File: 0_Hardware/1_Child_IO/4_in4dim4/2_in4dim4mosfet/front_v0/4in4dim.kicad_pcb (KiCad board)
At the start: 2 copper layers, 100.1 x 41.9 mm, 40 parts, among them IC1 ATTINY48-A, P1 CONN_8X2, P2 CONN_2, P3 CONN_2, P4 CONN_2, P5 CONN_2, P6 CONN_2, Q1 PNP, Q2 PNP, Q3 PNP, Q4 PNP, SW1 SKQGAKE010

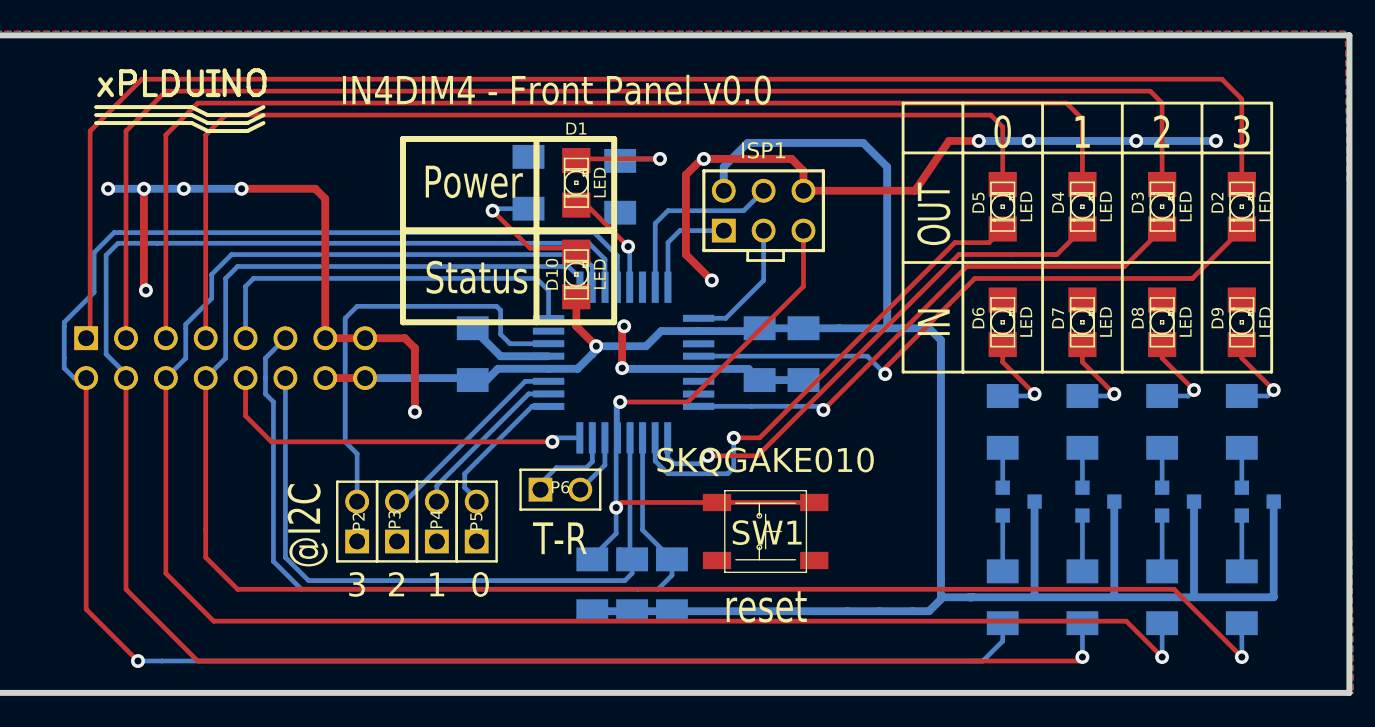
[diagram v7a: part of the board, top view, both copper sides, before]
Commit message: IN4DIM4: remplacement empreinte PNP par SOT-23 standard
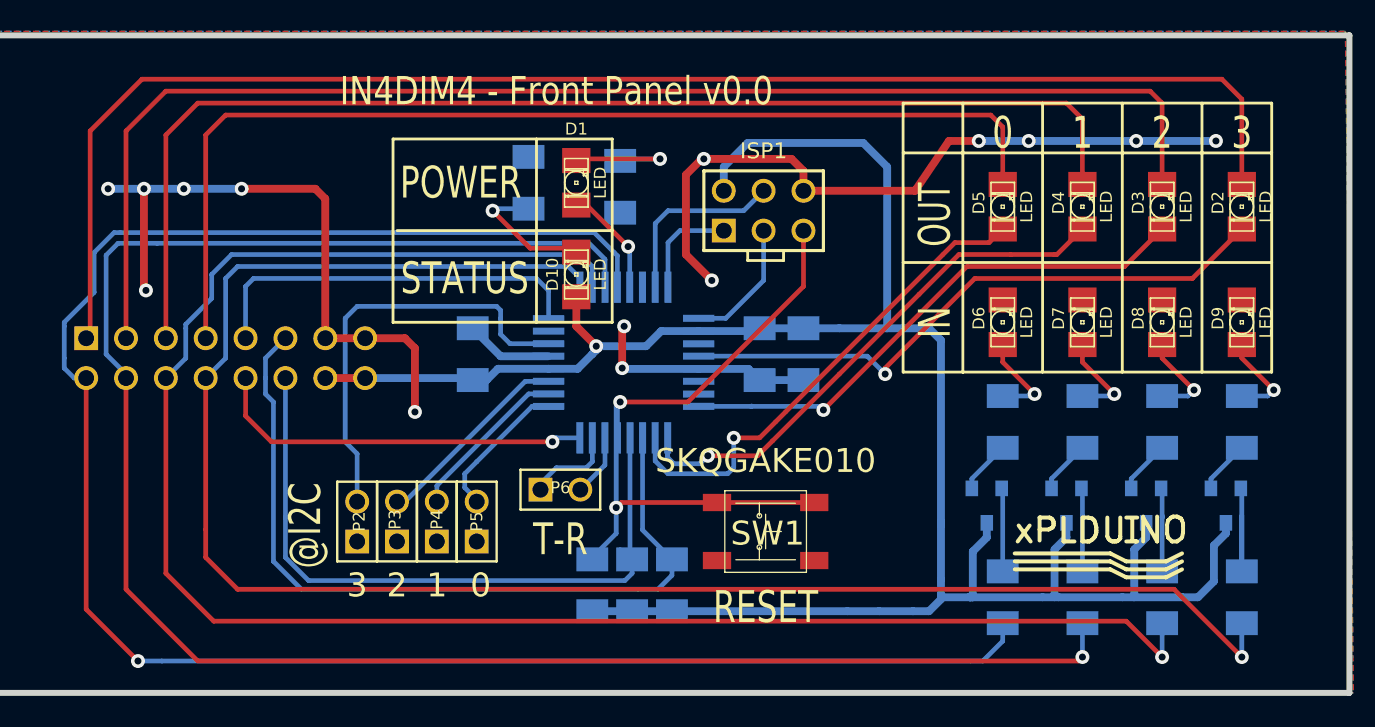
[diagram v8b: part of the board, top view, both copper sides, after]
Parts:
- Q1, Q2, Q3, Q4: footprint SOT23EBC -> SOT23
- moved logo_xplduino 65.1 mm to (186.4, 112.8)
- moved Q2 2.05 mm to (184.4, 109.5), turned to 0 degrees
- moved Q4 2.05 mm to (194.6, 109.5), turned to 0 degrees
- moved Q1 2.05 mm to (179.3, 109.5), turned to 0 degrees
- moved Q3 2.05 mm to (189.5, 109.5), turned to 0 degrees
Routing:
- net +5V: track 154.0 -> 145.5 mm
- net N-0000018: track 3.56 -> 8.87 mm
- net N-0000021: track 3.56 -> 5.44 mm
- net N-0000012: track 3.56 -> 5.44 mm
- net N-0000048: track 3.56 -> 5.32 mm
- net N-0000016: track 2.54 -> 3.40 mm
- net N-0000015: track 2.54 -> 3.40 mm
- net N-0000013: track 2.54 -> 3.40 mm
- net N-0000010: track 2.54 -> 3.40 mm
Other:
- board text added: "POWER"
- board text added: "RESET"
- board text added: "STATUS"
- board text removed: "Power"
- board text removed: "Status"
- board text removed: "reset"
